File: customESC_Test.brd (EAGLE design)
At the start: 152.4 x 127 mm, 61 parts, among them J1 3V3 -SWCLK-GND-SWDIO- NRST

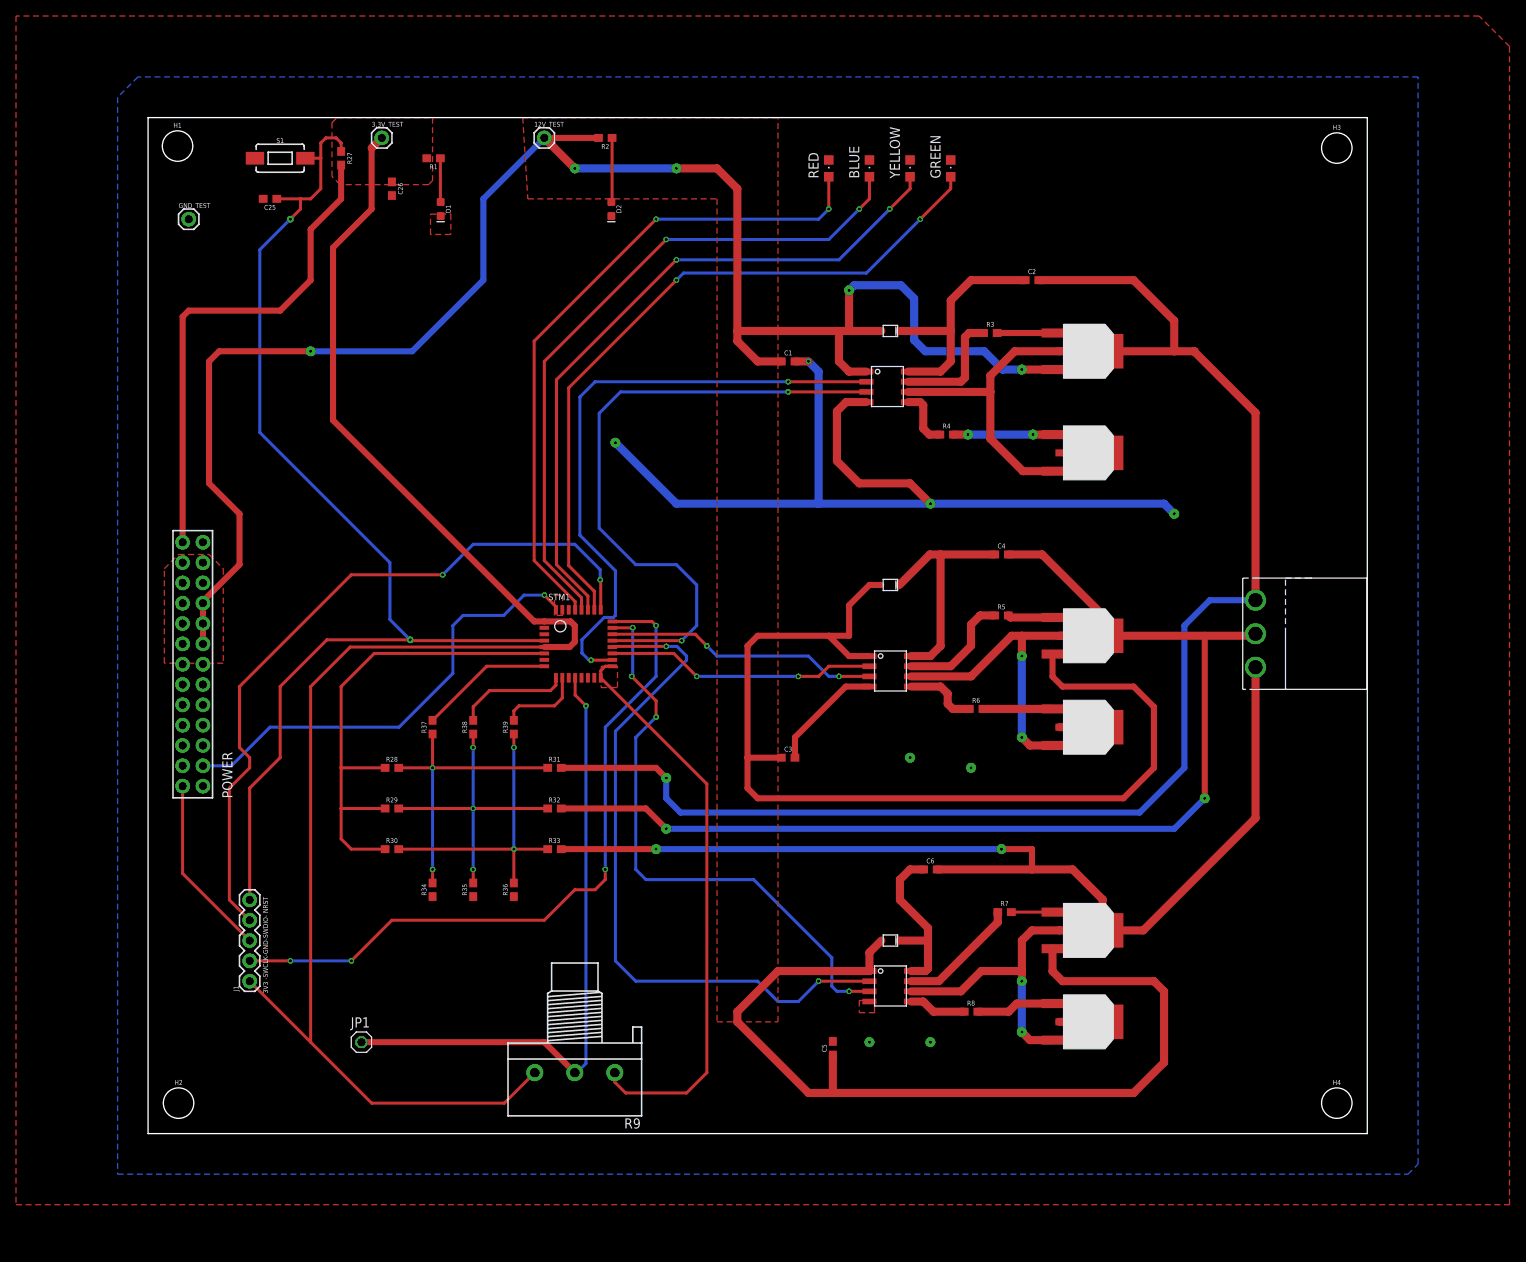
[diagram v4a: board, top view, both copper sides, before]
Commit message: updates on supply line and moved the leds and reset button
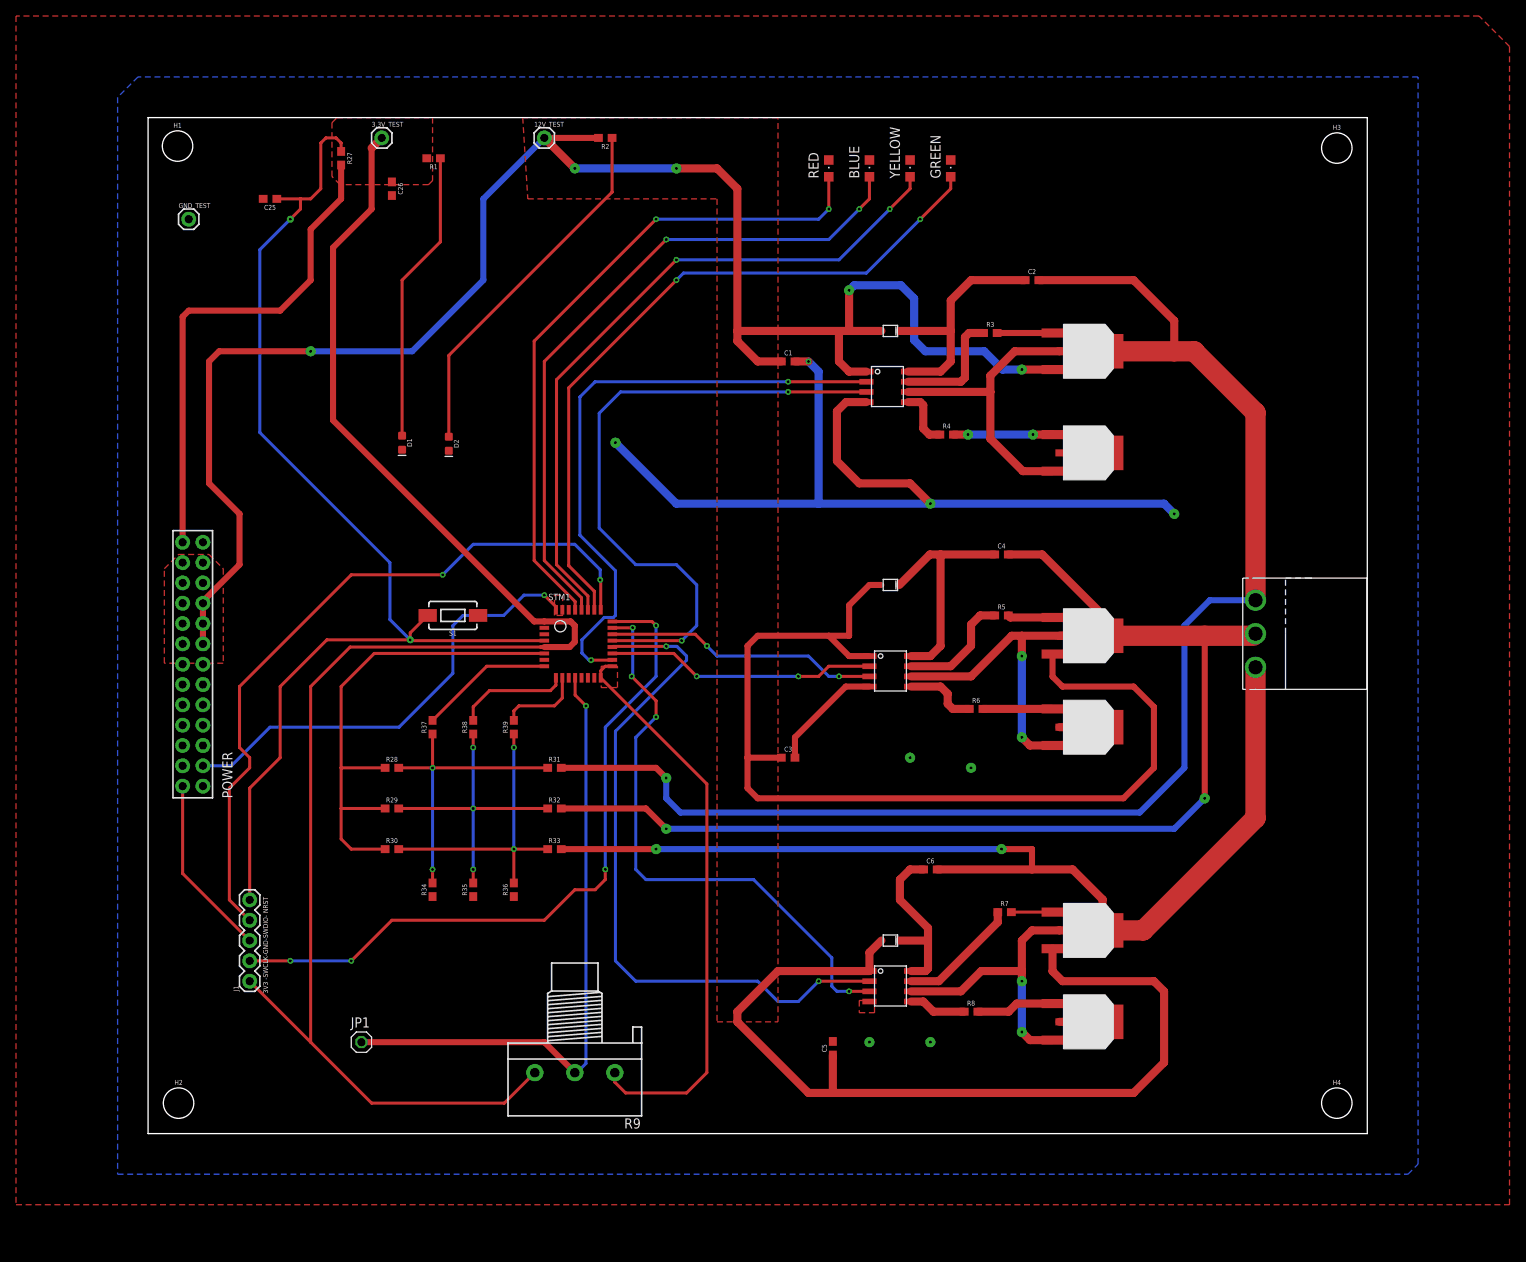
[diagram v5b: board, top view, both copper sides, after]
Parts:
- moved S1 61.1 mm to (38.1, 64.8), turned to 180 degrees
- moved D2 35.7 mm to (37.6, 86.2)
- moved D1 29.6 mm to (31.8, 86.4)
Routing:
- net N$2: track 8.05 -> 45.8 mm
- net N$1: track 5.49 -> 36.7 mm
- net NRST: track 146.6 -> 148.6 mm
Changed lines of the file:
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@@
 <drawing>
 <settings>
-<setting alwaysvectorfont="yes"/>
+<setting alwaysvectorfont="no"/>
 <setting verticaltext="up"/>
 </settings>
@@
 <attribute name="VALUE" x="97.79" y="32.258" size="0.6096" layer="27" font="vector" ratio="20" align="top-center"/>
 </element>
-<element name="D1" library="SparkFun-LED" library_urn="urn:adsk.eagle:library:529" package="LED-0603" package3d_urn="urn:adsk.eagle:package:39354/1" value="GREEN" x="36.576" y="115.57" smashed="yes" rot="R270">
-<attribute name="NAME" x="37.211" y="115.57" size="0.6096" layer="25" font="vector" ratio="20" rot="R270" align="bottom-center"/>
-<attribute name="PROD_ID" value="DIO-00821" x="-35.814" y="66.04" size="1.778" layer="27" rot="R270" display="off"/>
-<attribute name="VALUE" x="35.941" y="115.57" size="0.6096" layer="27" font="vector" ratio="20" rot="R270" align="top-center"/>
-</element>
-<element name="D2" library="SparkFun-LED" library_urn="urn:adsk.eagle:library:529" package="LED-0603" package3d_urn="urn:adsk.eagle:package:39354/1" value="GREEN" x="57.912" y="115.57" smashed="yes" rot="R270">
-<attribute name="NAME" x="58.547" y="115.57" size="0.6096" layer="25" font="vector" ratio="20" rot="R270" align="bottom-center"/>
-<attribute name="PROD_ID" value="DIO-00821" x="-14.478" y="62.23" size="1.778" layer="27" rot="R270" display="off"/>
-<attribute name="VALUE" x="57.277" y="115.57" size="0.6096" layer="27" font="vector" ratio="20" rot="R270" align="top-center"/>
+<element name="D1" library="SparkFun-LED" library_urn="urn:adsk.eagle:library:529" package="LED-0603" package3d_urn="urn:adsk.eagle:package:39354/1" value="GREEN" x="31.75" y="86.36" smashed="yes" rot="R270">
+<attribute name="NAME" x="32.385" y="86.36" size="0.6096" layer="25" font="vector" ratio="20" rot="R270" align="bottom-center"/>
+<attribute name="PROD_ID" value="DIO-00821" x="-40.64" y="36.83" size="1.778" layer="27" rot="R270" display="off"/>
+<attribute name="VALUE" x="31.115" y="86.36" size="0.6096" layer="27" font="vector" ratio="20" rot="R270" align="top-center"/>
+</element>
+<element name="D2" library="SparkFun-LED" library_urn="urn:adsk.eagle:library:529" package="LED-0603" package3d_urn="urn:adsk.eagle:package:39354/1" value="GREEN" x="37.592" y="86.233" smashed="yes" rot="R270">
+<attribute name="NAME" x="38.227" y="86.233" size="0.6096" layer="25" font="vector" ratio="20" rot="R270" align="bottom-center"/>
+<attribute name="PROD_ID" value="DIO-00821" x="-34.798" y="32.893" size="1.778" layer="27" rot="R270" display="off"/>
+<attribute name="VALUE" x="36.957" y="86.233" size="0.6096" layer="27" font="vector" ratio="20" rot="R270" align="top-center"/>
 </element>
 <element name="D3" library="X15-CustomESC" package="IN4148WS" value="IN4148WS" x="91.44" y="100.33" smashed="yes"/>
@@
 <attribute name="VALUE" x="102.87" y="14.478" size="0.6096" layer="27" font="vector" ratio="20" align="top-center"/>
 </element>
-<element name="S1" library="SparkFun-Switches" library_urn="urn:adsk.eagle:library:535" package="TACTILE_SWITCH_SMD_6.0X3.5MM" package3d_urn="urn:adsk.eagle:package:40165/1" value="MOMENTARY-SWITCH-SPST-SMD-6.0X3.5MM" x="16.51" y="121.92" smashed="yes">
-<attribute name="NAME" x="16.51" y="123.825" size="0.6096" layer="25" font="vector" ratio="20" align="bottom-center"/>
-<attribute name="PROD_ID" value="SWCH-00815" x="82.55" y="59.69" size="1.778" layer="27" display="off"/>
-<attribute name="SF_SKU" value="COM-08229" x="82.55" y="59.69" size="1.778" layer="27" display="off"/>
-<attribute name="VALUE" x="16.51" y="120.015" size="0.6096" layer="27" font="vector" ratio="20" align="top-center"/>
+<element name="S1" library="SparkFun-Switches" library_urn="urn:adsk.eagle:library:535" package="TACTILE_SWITCH_SMD_6.0X3.5MM" package3d_urn="urn:adsk.eagle:package:40165/1" value="MOMENTARY-SWITCH-SPST-SMD-6.0X3.5MM" x="38.1" y="64.77" smashed="yes" rot="R180">
+<attribute name="NAME" x="38.1" y="62.865" size="0.6096" layer="25" font="vector" ratio="20" rot="R180" align="bottom-center"/>
+<attribute name="PROD_ID" value="SWCH-00815" x="-27.94" y="127" size="1.778" layer="27" rot="R180" display="off"/>
+<attribute name="SF_SKU" value="COM-08229" x="-27.94" y="127" size="1.778" layer="27" rot="R180" display="off"/>
+<attribute name="VALUE" x="38.1" y="66.675" size="0.6096" layer="27" font="vector" ratio="20" rot="R180" align="top-center"/>
 </element>
 <element name="STM1" library="X15-CustomESC" package="STM32F042K6T6" value="STM32F042K6T6" x="49.53" y="58.42" smashed="yes">
@@
 <contactref element="R1" pad="1"/>
 <contactref element="D1" pad="A"/>
-<wire x1="36.576" y1="116.447" x2="36.537" y2="116.486" width="0.381" layer="1"/>
-<wire x1="36.537" y1="116.486" x2="36.537" y2="121.92" width="0.381" layer="1"/>
+<wire x1="36.537" y1="121.92" x2="36.537" y2="111.467" width="0.381" layer="1"/>
+<wire x1="36.537" y1="111.467" x2="31.75" y2="106.68" width="0.381" layer="1"/>
+<wire x1="31.75" y1="106.68" x2="31.75" y2="87.237" width="0.381" layer="1"/>
 </signal>
 <signal name="N$2">
 <contactref element="R2" pad="1"/>
 <contactref element="D2" pad="A"/>
-<wire x1="57.912" y1="116.447" x2="58" y2="116.535" width="0.381" layer="1"/>
-<wire x1="58" y1="116.535" x2="58" y2="124.46" width="0.381" layer="1"/>
+<wire x1="58" y1="117.678" x2="37.592" y2="97.27" width="0.381" layer="1"/>
+<wire x1="37.592" y1="87.11" x2="37.592" y2="97.27" width="0.381" layer="1"/>
+<wire x1="58" y1="117.678" x2="58" y2="124.46" width="0.381" layer="1"/>
 </signal>
 <signal name="VCC_1">
@@
 <vertex x="90.678" y="16.637"/>
 </polygon>
-<polygon width="0.381" layer="1">
-<vertex x="35.306" y="114.935"/>
-<vertex x="37.846" y="114.935"/>
-<vertex x="37.846" y="112.395"/>
-<vertex x="35.306" y="112.395"/>
-</polygon>
 <contactref element="R9" pad="1"/>
 <contactref element="RED" pad="C"/>
@@
 <contactref element="C2" pad="2"/>
 <contactref element="R31" pad="2"/>
-<wire x1="119.3165" y1="97.79" x2="128.27" y2="97.79" width="1.016" layer="1"/>
-<wire x1="128.27" y1="97.79" x2="130.81" y2="97.79" width="1.016" layer="1"/>
-<wire x1="130.77825" y1="97.75825" x2="138.43" y2="90.1065" width="1.016" layer="1"/>
+<wire x1="119.3165" y1="97.79" x2="128.27" y2="97.79" width="2.54" layer="1"/>
+<wire x1="128.27" y1="97.79" x2="130.81" y2="97.79" width="2.54" layer="1"/>
+<wire x1="130.77825" y1="97.75825" x2="138.43" y2="90.1065" width="2.54" layer="1"/>
 <wire x1="113.919" y1="97.79" x2="108.331" y2="97.79" width="1.016" layer="1"/>
 <wire x1="108.331" y1="97.79" x2="105.283" y2="94.742" width="1.016" layer="1"/>
@@
 <wire x1="66.548" y1="40.132" x2="64.77" y2="41.91" width="0.762" layer="16"/>
 <wire x1="64.77" y1="41.91" x2="64.77" y2="44.45" width="0.762" layer="16"/>
-<wire x1="138.43" y1="90.1065" x2="138.43" y2="66.675" width="1.016" layer="1"/>
+<wire x1="138.43" y1="90.1065" x2="138.43" y2="66.675" width="2.54" layer="1"/>
 </signal>
 <signal name="PHASE_B1">
@@
 <contactref element="R32" pad="2"/>
 <wire x1="138.176" y1="62.23" x2="138.43" y2="62.484" width="1.016" layer="1"/>
-<wire x1="119.3165" y1="62.23" x2="132.08" y2="62.23" width="1.016" layer="1"/>
-<wire x1="132.08" y1="62.23" x2="138.176" y2="62.23" width="1.016" layer="1"/>
+<wire x1="119.3165" y1="62.23" x2="132.08" y2="62.23" width="2.54" layer="1"/>
+<wire x1="132.08" y1="62.23" x2="138.176" y2="62.23" width="2.54" layer="1"/>
 <wire x1="107.53" y1="72.39" x2="111.76" y2="72.39" width="1.016" layer="1"/>
 <wire x1="119.3165" y1="64.8335" x2="119.3165" y2="62.23" width="1.016" layer="1"/>
@@
 <wire x1="104.14" y1="20.32" x2="109.22" y2="20.32" width="1.016" layer="1"/>
 <via x="109.22" y="19.05" extent="1-16" drill="0.35" diameter="1.3"/>
-<wire x1="138.43" y1="39.4335" x2="124.3965" y2="25.4" width="1.016" layer="1"/>
-<wire x1="119.3165" y1="25.4" x2="124.3965" y2="25.4" width="1.016" layer="1"/>
-<wire x1="138.43" y1="39.4335" x2="138.43" y2="58.293" width="1.016" layer="1"/>
+<wire x1="138.43" y1="39.4335" x2="124.3965" y2="25.4" width="2.54" layer="1"/>
+<wire x1="119.3165" y1="25.4" x2="124.3965" y2="25.4" width="2.54" layer="1"/>
+<wire x1="138.43" y1="39.4335" x2="138.43" y2="58.293" width="2.54" layer="1"/>
 <wire x1="110.236" y1="11.684" x2="109.22" y2="12.7" width="1.016" layer="1"/>
 <via x="109.22" y="12.7" extent="1-16" drill="0.35" diameter="1.3"/>
@@
 <wire x1="23.495" y1="124.46" x2="22.225" y2="124.46" width="0.381" layer="1"/>
 <wire x1="22.225" y1="124.46" x2="21.59" y2="123.825" width="0.381" layer="1"/>
-<wire x1="21.59" y1="123.825" x2="21.59" y2="121.92" width="0.381" layer="1"/>
 <wire x1="24.13" y1="123.825" x2="23.495" y2="124.46" width="0.381" layer="1"/>
 <wire x1="32.766" y1="61.62" x2="32.766" y2="61.722" width="0.381" layer="1"/>
@@
 <wire x1="21.59" y1="118.11" x2="20.32" y2="116.84" width="0.381" layer="1"/>
 <wire x1="20.32" y1="116.84" x2="19.05" y2="116.84" width="0.381" layer="1"/>
-<wire x1="21.59" y1="121.92" x2="21.59" y2="118.11" width="0.381" layer="1"/>
-<wire x1="19.66" y1="121.92" x2="21.59" y2="121.92" width="0.381" layer="1"/>
+<wire x1="21.59" y1="123.825" x2="21.59" y2="118.11" width="0.381" layer="1"/>
 <contactref element="J1" pad="5"/>
 <wire x1="12.7" y1="29.21" x2="12.7" y2="43.18" width="0.381" layer="1"/>
@@
 <wire x1="16.51" y1="55.88" x2="22.352" y2="61.722" width="0.381" layer="1"/>
 <wire x1="22.352" y1="61.722" x2="32.766" y2="61.722" width="0.381" layer="1"/>
+<wire x1="34.95" y1="64.77" x2="32.766" y2="62.586" width="0.381" layer="1"/>
+<wire x1="32.766" y1="62.586" x2="32.766" y2="61.722" width="0.381" layer="1"/>
 </signal>
 <signal name="COM1">

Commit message: Fixed it Raghav
Hi
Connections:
- net PWM_IN: no longer R9.2
- net TIM1: now also R9.2
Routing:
- net TIM1: track 0.00 -> 51.8 mm, vias 0 -> 1
- net PWM_IN: track 78.9 -> 65.1 mm, vias 1 -> 2
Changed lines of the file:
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@@
 <signal name="TIM1">
 <contactref element="STM1" pad="PB0"/>
+<contactref element="R9" pad="2"/>
+<wire x1="54.98" y1="56.97" x2="54.98" y2="54.621" width="0.381" layer="1"/>
+<wire x1="54.98" y1="54.621" x2="55.88" y2="53.721" width="0.381" layer="1"/>
+<wire x1="55.88" y1="53.721" x2="55.88" y2="53.34" width="0.381" layer="1"/>
+<via x="55.88" y="53.34" extent="1-16" drill="0.35"/>
+<wire x1="55.88" y1="53.34" x2="55.88" y2="31.75" width="0.381" layer="16"/>
+<wire x1="55.88" y1="31.75" x2="57.15" y2="30.48" width="0.381" layer="16"/>
+<wire x1="57.15" y1="30.48" x2="57.15" y2="11.43" width="0.381" layer="16"/>
+<wire x1="57.15" y1="11.43" x2="53.34" y2="7.62" width="0.381" layer="16"/>
 </signal>
 <signal name="NRST">
@@
 </signal>
 <signal name="PWM_IN">
-<contactref element="R9" pad="2"/>
 <contactref element="STM1" pad="PA6"/>
 <contactref element="JP1" pad="1"/>
-<wire x1="54.737" y1="8.763" x2="53.594" y2="7.62" width="0.381" layer="16"/>
-<wire x1="53.34" y1="7.62" x2="53.594" y2="7.62" width="0.381" layer="16"/>
-<via x="54.737" y="53.467" extent="1-16" drill="0.35"/>
-<wire x1="53.38" y1="56.97" x2="53.38" y2="54.824" width="0.381" layer="1"/>
-<wire x1="53.38" y1="54.824" x2="54.737" y2="53.467" width="0.381" layer="1"/>
-<wire x1="54.737" y1="8.763" x2="54.737" y2="53.467" width="0.381" layer="16"/>
-<wire x1="26.67" y1="11.43" x2="49.53" y2="11.43" width="0.762" layer="1"/>
-<wire x1="49.53" y1="11.43" x2="53.34" y2="7.62" width="0.762" layer="1"/>
+<via x="54.61" y="52.705" extent="1-16" drill="0.35"/>
+<wire x1="53.38" y1="56.97" x2="53.38" y2="53.935" width="0.381" layer="1"/>
+<wire x1="53.38" y1="53.935" x2="54.61" y2="52.705" width="0.381" layer="1"/>
+<wire x1="38.1" y1="22.86" x2="50.8" y2="22.86" width="0.762" layer="1"/>
+<wire x1="26.67" y1="11.43" x2="38.1" y2="22.86" width="0.762" layer="1"/>
+<wire x1="54.61" y1="26.67" x2="50.8" y2="22.86" width="0.762" layer="1"/>
+<via x="54.61" y="26.67" extent="1-16" drill="0.55"/>
+<wire x1="54.61" y1="52.705" x2="54.61" y2="26.67" width="0.762" layer="16"/>
 </signal>
 <signal name="TEST_LED4">
